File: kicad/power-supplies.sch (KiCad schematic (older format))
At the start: 16 parts, among them J2 BARREL_JACK, U3 AP3211

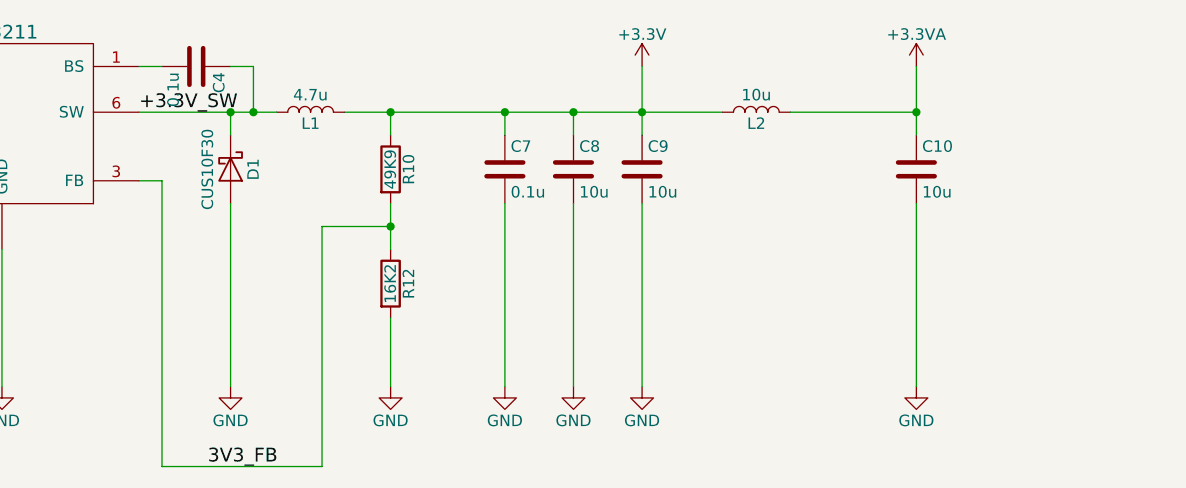
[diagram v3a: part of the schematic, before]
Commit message: Removed comp, efuse. Added zener protection. Fixed OLED footprint.
I may have destroyed a board by shorting the FB pin to ground. I left
off the zener protection on Rev A. Never again.
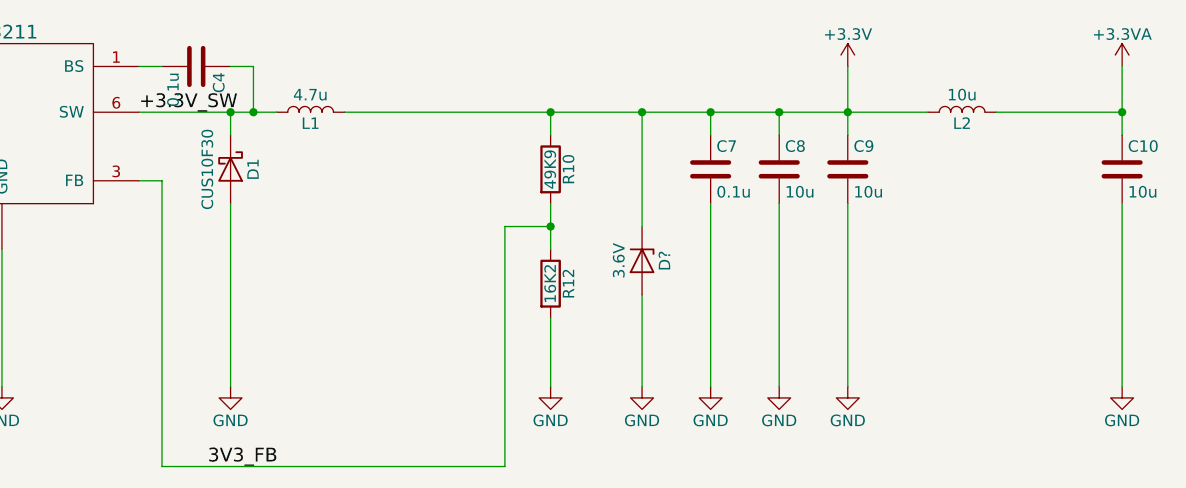
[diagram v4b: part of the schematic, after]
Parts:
- added D?: 3.6V, Diodes_SMD:D_SOD-523, symbol D_Zener
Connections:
- net +3V3: now also D?.1 (K)
- net GND: now also D?.2 (A)
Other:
- moved on the sheet: C10, C7, C8, C9, L2, R10, R12

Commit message: Added overvoltage protection circuit to +3.3V
Part selection is complete. There are things without part numbers.

It uses a TL431 as a precision comparator with integrated voltage
reference to activate a latch which both shuts down the regulator and
throws a crobar across +3.3V. There is also space for a fuse on +3.3V
(I'm thinking a PTC resettable fuse could go there, but I'm not sure
what the tradeoffs are for that).
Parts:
- added D4: NYC228STT1G, TO_SOT_Packages_SMD:SOT-223-3Lead_TabPin2, symbol Q_Thyristor_KAG
- added F1: Fuse_Small, symbol Fuse_Small
- added Q4: Q_PNP_BCE, symbol Q_PNP_BCE
- added Q5: FDG6301N_F085, TO_SOT_Packages_SMD:SOT-363_SC-70-6, symbol Q_NMOS_SGD_DUAL
- added R21, R23, R24, R25: 10K, Resistors_SMD:R_0402, symbol R
- added R22: 1K, symbol R
- added R26: 22K6, Resistors_SMD:R_0402, symbol R
- added U7: TL431, TO_SOT_Packages_SMD:SOT-323_SC-70, symbol TL431
- gave numbers to parts that had none: 1
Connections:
- net +12V: now also Q4.3 (E), R21.1
- net +3V3: now also D4.2 (A), F1.2, R24.1; no longer L1.2
- net GND: now also D4.1 (K), Q5.1 (S), Q5.4 (S), R25.2, R26.2, U7.6
- net +3.3V_EN: now reaches R11.1, R9.2, U3.4 (EN)
- net +3.3V_EN: now also Q5.6 (D)
- new net: F1.1, L1.2
- new net: Q4.2 (C), R23.1
- new net OVP_LATCH_IN: Q4.1 (B), R21.2, R22.1
- new net OVP_LATCH_OUT: D4.3 (G), Q5.2 (G), Q5.5 (G), R23.2, R25.1
- new net OVP_LATCH_REG: Q5.3 (D), R22.2, U7.1
- new net OVP_LATCH_TRIP: R24.2, R26.1, U7.3
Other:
- note added: "Alternate mosfet part: 2N7002DWCT-ND"
- note added: "Trip point 3.6V"
- note added: "Zener is optional and is a fallback if the OVP circuit does not operate\nas expected.\n\nThe OVP circuit uses a TL431 as a precision comparator with integrated\nvoltage reference to set off a latch which both disables EN and throws\nan SCR crowbar on +3.3V until 12V is removed."

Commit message: Added overtemperature latching circuit with reset
This uses a comparator to trigger the same latch type that is used on
the OVP circuit.
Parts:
- R22: footprint (none) -> Resistors_SMD:R_0402; Part No. (none) -> 311-1.0KJRCT-ND
- U7: footprint TO_SOT_Packages_SMD:SOT-323_SC-70 -> TO_SOT_Packages_SMD:SOT-363_SC-70-6
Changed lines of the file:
@@
 $EndComp
 $Comp
-L GND #PWR22
+L GND #PWR023
 U 1 1 592084EC
 P 1600 1900
-F 0 "#PWR22" H 1600 1650 50  0001 C CNN
+F 0 "#PWR023" H 1600 1650 50  0001 C CNN
 F 1 "GND" H 1600 1750 50  0000 C CNN
 F 2 "" H 1600 1900 50  0001 C CNN
@@
 $EndComp
 $Comp
-L +12V #PWR21
+L +12V #PWR024
 U 1 1 59208505
 P 1600 1200
-F 0 "#PWR21" H 1600 1050 50  0001 C CNN
+F 0 "#PWR024" H 1600 1050 50  0001 C CNN
 F 1 "+12V" H 1600 1340 50  0000 C CNN
 F 2 "" H 1600 1200 50  0001 C CNN
@@
 $EndComp
 $Comp
-L GND #PWR27
+L GND #PWR025
 U 1 1 592088C5
 P 5500 2500
-F 0 "#PWR27" H 5500 2250 50  0001 C CNN
+F 0 "#PWR025" H 5500 2250 50  0001 C CNN
 F 1 "GND" H 5500 2350 50  0000 C CNN
 F 2 "" H 5500 2500 50  0001 C CNN
@@
 $EndComp
 $Comp
-L GND #PWR26
+L GND #PWR026
 U 1 1 59208941
 P 4500 2500
-F 0 "#PWR26" H 4500 2250 50  0001 C CNN
+F 0 "#PWR026" H 4500 2250 50  0001 C CNN
 F 1 "GND" H 4500 2350 50  0000 C CNN
 F 2 "" H 4500 2500 50  0001 C CNN
@@
 $EndComp
 $Comp
-L +3.3V #PWR19
+L +3.3V #PWR027
 U 1 1 59208C89
 P 8200 1100
-F 0 "#PWR19" H 8200 950 50  0001 C CNN
+F 0 "#PWR027" H 8200 950 50  0001 C CNN
 F 1 "+3.3V" H 8200 1240 50  0000 C CNN
 F 2 "" H 8200 1100 50  0001 C CNN
@@
 $EndComp
 $Comp
-L GND #PWR32
+L GND #PWR028
 U 1 1 59208D24
 P 8200 2500
-F 0 "#PWR32" H 8200 2250 50  0001 C CNN
+F 0 "#PWR028" H 8200 2250 50  0001 C CNN
 F 1 "GND" H 8200 2350 50  0000 C CNN
 F 2 "" H 8200 2500 50  0001 C CNN
@@
 $EndComp
 $Comp
-L GND #PWR23
+L GND #PWR029
 U 1 1 59208EA1
 P 3150 2500
-F 0 "#PWR23" H 3150 2250 50  0001 C CNN
+F 0 "#PWR029" H 3150 2250 50  0001 C CNN
 F 1 "GND" H 3150 2350 50  0000 C CNN
 F 2 "" H 3150 2500 50  0001 C CNN
@@
 $EndComp
 $Comp
-L GND #PWR30
+L GND #PWR030
 U 1 1 5920907B
 P 7600 2500
-F 0 "#PWR30" H 7600 2250 50  0001 C CNN
+F 0 "#PWR030" H 7600 2250 50  0001 C CNN
 F 1 "GND" H 7600 2350 50  0000 C CNN
 F 2 "" H 7600 2500 50  0001 C CNN
@@
 $EndComp
 $Comp
-L GND #PWR24
+L GND #PWR031
 U 1 1 592091A5
 P 3400 2500
-F 0 "#PWR24" H 3400 2250 50  0001 C CNN
+F 0 "#PWR031" H 3400 2250 50  0001 C CNN
 F 1 "GND" H 3400 2350 50  0000 C CNN
 F 2 "" H 3400 2500 50  0001 C CNN
@@
 $EndComp
 $Comp
-L GND #PWR28
+L GND #PWR032
 U 1 1 592093A2
 P 6900 2500
-F 0 "#PWR28" H 6900 2250 50  0001 C CNN
+F 0 "#PWR032" H 6900 2250 50  0001 C CNN
 F 1 "GND" H 6900 2350 50  0000 C CNN
 F 2 "" H 6900 2500 50  0001 C CNN
@@
 $EndComp
 $Comp
-L GND #PWR25
+L GND #PWR033
 U 1 1 59209C78
 P 3700 2500
-F 0 "#PWR25" H 3700 2250 50  0001 C CNN
+F 0 "#PWR033" H 3700 2250 50  0001 C CNN
 F 1 "GND" H 3700 2350 50  0000 C CNN
 F 2 "" H 3700 2500 50  0001 C CNN
@@
 $EndComp
 $Comp
-L GND #PWR31
+L GND #PWR034
 U 1 1 5920A4A0
 P 7900 2500
-F 0 "#PWR31" H 7900 2250 50  0001 C CNN
+F 0 "#PWR034" H 7900 2250 50  0001 C CNN
 F 1 "GND" H 7900 2350 50  0000 C CNN
 F 2 "" H 7900 2500 50  0001 C CNN
@@
 $EndComp
 $Comp
-L GND #PWR33
+L GND #PWR035
 U 1 1 592C8FE8
 P 9400 2500
-F 0 "#PWR33" H 9400 2250 50  0001 C CNN
+F 0 "#PWR035" H 9400 2250 50  0001 C CNN
 F 1 "GND" H 9400 2350 50  0000 C CNN
 F 2 "" H 9400 2500 50  0001 C CNN
@@
 $EndComp
 $Comp
-L +3.3VA #PWR20
+L +3.3VA #PWR036
 U 1 1 592C9106
 P 9400 1100
-F 0 "#PWR20" H 9400 950 50  0001 C CNN
+F 0 "#PWR036" H 9400 950 50  0001 C CNN
 F 1 "+3.3VA" H 9400 1240 50  0000 C CNN
 F 2 "" H 9400 1100 50  0001 C CNN
@@
 $EndComp
 $Comp
-L GND #PWR29
+L GND #PWR037
 U 1 1 5987D189
 P 7300 2500
-F 0 "#PWR29" H 7300 2250 50  0001 C CNN
+F 0 "#PWR037" H 7300 2250 50  0001 C CNN
 F 1 "GND" H 7300 2350 50  0000 C CNN
 F 2 "" H 7300 2500 50  0001 C CNN
@@
 F 0 "U7" H 2300 4950 60  0000 C CNN
 F 1 "TL431" H 2400 5300 60  0000 C CNN
-F 2 "TO_SOT_Packages_SMD:SOT-323_SC-70" H 2200 5150 60  0001 C CNN
+F 2 "TO_SOT_Packages_SMD:SOT-363_SC-70-6" H 2200 5150 60  0001 C CNN
 F 3 "" H 2200 5150 60  0001 C CNN
 F 4 "296-17863-1-ND" H 2200 5150 60  0001 C CNN "Part No."
@@
 F 0 "R22" V 2280 4550 50  0000 C CNN
 F 1 "1K" V 2200 4550 50  0000 C CNN
-F 2 "" V 2130 4550 50  0001 C CNN
+F 2 "Resistors_SMD:R_0402" V 2130 4550 50  0001 C CNN
 F 3 "" H 2200 4550 50  0001 C CNN
+F 4 "311-1.0KJRCT-ND" H 2200 4550 60  0001 C CNN "Part No."
 	1    2200 4550
 	-1   0    0    -1
 $EndComp
 $Comp
-L GND #PWR37
+L GND #PWR038
 U 1 1 5998FEAD
 P 2200 5800
-F 0 "#PWR37" H 2200 5550 50  0001 C CNN
+F 0 "#PWR038" H 2200 5550 50  0001 C CNN
 F 1 "GND" H 2200 5650 50  0000 C CNN
 F 2 "" H 2200 5800 50  0001 C CNN
@@
 Trip point 3.6V
 $Comp
-L +12V #PWR34
+L +12V #PWR039
 U 1 1 599906B9
 P 3600 3700
-F 0 "#PWR34" H 3600 3550 50  0001 C CNN
+F 0 "#PWR039" H 3600 3550 50  0001 C CNN
 F 1 "+12V" H 3600 3840 50  0000 C CNN
 F 2 "" H 3600 3700 50  0001 C CNN
@@
 $EndComp
 $Comp
-L +3.3V #PWR36
+L +3.3V #PWR040
 U 1 1 59991F79
 P 1700 4600
-F 0 "#PWR36" H 1700 4450 50  0001 C CNN
+F 0 "#PWR040" H 1700 4450 50  0001 C CNN
 F 1 "+3.3V" H 1700 4740 50  0000 C CNN
 F 2 "" H 1700 4600 50  0001 C CNN
@@
 	1600 1200 1600 1300
 Wire Wire Line
-	5100 1300 5500 1300
-Wire Wire Line
-	5500 1300 5600 1300
-Wire Wire Line
-	5600 1300 5700 1300
+	5100 1300 5700 1300
 Wire Wire Line
 	5200 1100 5100 1100
@@
 	1500 1500 1600 1500
 Wire Wire Line
-	1500 1300 1600 1300
-Wire Wire Line
-	1600 1300 3150 1300
-Wire Wire Line
-	3150 1300 3400 1300
-Wire Wire Line
-	3400 1300 3700 1300
-Wire Wire Line
-	3700 1300 3900 1300
+	1500 1300 3900 1300
 Wire Wire Line
 	4500 2500 4500 1900
 Connection ~ 1600 1300
 Wire Wire Line
-	8200 1100 8200 1300
-Wire Wire Line
-	8200 1300 8200 1400
+	8200 1100 8200 1400
 Connection ~ 7900 1300
 Wire Wire Line
@@
 Connection ~ 3150 1300
 Wire Wire Line
-	7600 1400 7600 1300
+	7600 1300 7600 1400
 Connection ~ 7600 1300
 Wire Wire Line
@@
 	6900 2500 6900 2200
 Wire Wire Line
-	6900 1700 6900 1800
-Wire Wire Line
-	6900 1800 6900 1900
+	6900 1700 6900 1900
 Wire Wire Line
 	6900 1400 6900 1300
@@
 	3700 1300 3700 1400
 Wire Wire Line
-	3700 1700 3700 1800
-Wire Wire Line
-	3700 1800 3700 1900
+	3700 1700 3700 1900
 Wire Wire Line
 	3700 2500 3700 2200
@@
 Connection ~ 8200 1300
 Wire Wire Line
-	7900 1400 7900 1300
+	7900 1300 7900 1400
 Wire Wire Line
 	7900 2500 7900 1700
 Wire Wire Line
-	9400 1100 9400 1300
-Wire Wire Line
-	9400 1300 9400 1400
+	9400 1100 9400 1400
 Wire Wire Line
 	9400 1700 9400 2500
@@
 Connection ~ 9400 1300
 Wire Wire Line
-	7300 1800 7300 1300
+	7300 1300 7300 1800
 Connection ~ 7300 1300
 Wire Wire Line
@@
 	3300 4300 2200 4300
 Wire Wire Line
-	2200 4200 2200 4300
-Wire Wire Line
-	2200 4300 2200 4400
-Wire Wire Line
-	2200 4700 2200 4800
-Wire Wire Line
-	2200 4800 2200 4850
-Wire Wire Line
-	2200 5500 2200 5600
-Wire Wire Line
-	2200 5600 2200 5700
-Wire Wire Line
-	2200 5700 2200 5800
+	2200 4200 2200 4400
+Wire Wire Line
+	2200 4700 2200 4850
+Wire Wire Line
+	2200 5500 2200 5800
 Wire Wire Line
 	2200 5700 1700 5700
@@
 	1900 5200 1700 5200
 Wire Wire Line
-	1700 5100 1700 5200
-Wire Wire Line
-	1700 5200 1700 5300
+	1700 5100 1700 5300
 Connection ~ 1700 5200
 Wire Wire Line
-	3600 3700 3600 3800
-Wire Wire Line
-	3600 3800 3600 4100
+	3600 3700 3600 4100
 Wire Wire Line
 	3600 3800 2200 3800
@@
 Connection ~ 2200 4300
 Wire Wire Line
-	2200 5600 3000 5600
-Wire Wire Line
-	3000 5600 3600 5600
-Wire Wire Line
-	3600 5600 4900 5600
-Wire Wire Line
-	4900 5600 5750 5600
+	2200 5600 5750 5600
 Wire Wire Line
 	3600 5600 3600 5500
@@
 Connection ~ 3000 5600
 Wire Wire Line
-	3600 4900 3600 5000
-Wire Wire Line
-	3600 5000 3600 5100
-Wire Wire Line
-	3600 5100 3600 5200
+	3600 4900 3600 5200
 Wire Wire Line
 	3600 5100 3300 5100
@@
 Connection ~ 3600 5600
 Wire Wire Line
-	3600 5000 4600 5000
-Wire Wire Line
-	4600 5000 5600 5000
+	3600 5000 5600 5000
 Connection ~ 3600 5000
 Wire Wire Line
@@
 $EndComp
 $Comp
-L +3.3V #PWR35
+L +3.3V #PWR041
 U 1 1 599981D4
 P 5750 4400
-F 0 "#PWR35" H 5750 4250 50  0001 C CNN
+F 0 "#PWR041" H 5750 4250 50  0001 C CNN
 F 1 "+3.3V" H 5750 4540 50  0000 C CNN
 F 2 "" H 5750 4400 50  0001 C CNN
@@
 	5750 4400 5750 4750
 Wire Wire Line
-	3850 1600 3850 1800
-Wire Wire Line
-	3850 1800 3850 2900
+	3850 1600 3850 2900
 Wire Wire Line
 	4900 4800 4900 2900
@@
 	6000 1300 6200 1300
 Wire Wire Line
-	6400 1300 6900 1300
-Wire Wire Line
-	6900 1300 7300 1300
-Wire Wire Line
-	7300 1300 7600 1300
-Wire Wire Line
-	7600 1300 7900 1300
-Wire Wire Line
-	7900 1300 8200 1300
-Wire Wire Line
-	8200 1300 8550 1300
+	6400 1300 8550 1300
 Text Notes 6300 4200 0    60   ~ 0
 Zener is optional and is a fallback if the OVP circuit does not operate\nas expected.\n\nThe OVP circuit uses a TL431 as a precision comparator with integrated\nvoltage reference to set off a latch which both disables EN and throws\nan SCR crowbar on +3.3V until 12V is removed.

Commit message: Fixed thermal cutoff circuit and finished footprint selection
The main issue with the thermal cutoff was the open-collector maximum
voltage. I had to find a (slightly more expensive) comparator with an
output that was tolerant. Other comparators that would be instead
tolerant of being run off 12V were about the same price.

The fuse I'm not sure about. I'm just going to short it out. The
regulator can handle a short circuit and so can the crowbar. I also
couldn't decide where to put the feedback network. If I put it after the
fuse it would compensate for any voltage drop across it. However, it
would also cause the regulator to try to boost the voltage insanely high
during a short circuit across the fuse and maybe cause it to pop (I
could really only find ones rated to 6V). I instead placed it before the
fuse. I'm still not sure.
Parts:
- removed Q4: Q_PNP_BCE, symbol Q_PNP_BCE
- added Q4: MMBT3906WT1G, TO_SOT_Packages_SMD:SOT-323_SC-70, symbol Q_PNP_BEC
- F1: footprint (none) -> Resistors_SMD:R_0603
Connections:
- net +12V: now also Q4.2 (E)
- net +3V3: no longer R10.1
- net OVP_LATCH_IN: now also Q4.1 (B)
- net at F1.1, L1.2: now also R10.1
- net at R23.1: now also Q4.3 (C)
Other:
- note added: "The fuse here is probably optional. I will replace it with\na short, but the 0603 footprint should allow a standard\nSMD fuse or PTC thermistor in its place.\n\nThe AP3211 should handle a short circuit condition and\nshut down. The crowbar can sustain the 1.5A maximum\ncurrent."
- moved on the sheet: C10, C4, C5, C6, C7, C8, C9, D1, D3, F1, J2, L1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

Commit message: Changed out switch for two small side clicker ones
Should make things a little easier to lay out and easier to modify
later.
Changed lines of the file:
@@
 $EndComp
 $Comp
-L GND #PWR023
+L GND #PWR26
 U 1 1 592084EC
 P 1600 2100
-F 0 "#PWR023" H 1600 1850 50  0001 C CNN
+F 0 "#PWR26" H 1600 1850 50  0001 C CNN
 F 1 "GND" H 1600 1950 50  0000 C CNN
 F 2 "" H 1600 2100 50  0001 C CNN
@@
 $EndComp
 $Comp
-L +12V #PWR024
+L +12V #PWR25
 U 1 1 59208505
 P 1600 1400
-F 0 "#PWR024" H 1600 1250 50  0001 C CNN
+F 0 "#PWR25" H 1600 1250 50  0001 C CNN
 F 1 "+12V" H 1600 1540 50  0000 C CNN
 F 2 "" H 1600 1400 50  0001 C CNN
@@
 $EndComp
 $Comp
-L GND #PWR025
+L GND #PWR31
 U 1 1 592088C5
 P 5500 2700
-F 0 "#PWR025" H 5500 2450 50  0001 C CNN
+F 0 "#PWR31" H 5500 2450 50  0001 C CNN
 F 1 "GND" H 5500 2550 50  0000 C CNN
 F 2 "" H 5500 2700 50  0001 C CNN
@@
 $EndComp
 $Comp
-L GND #PWR026
+L GND #PWR30
 U 1 1 59208941
 P 4500 2700
-F 0 "#PWR026" H 4500 2450 50  0001 C CNN
+F 0 "#PWR30" H 4500 2450 50  0001 C CNN
 F 1 "GND" H 4500 2550 50  0000 C CNN
 F 2 "" H 4500 2700 50  0001 C CNN
@@
 $EndComp
 $Comp
-L +3.3V #PWR027
+L +3.3V #PWR23
 U 1 1 59208C89
 P 8200 1300
-F 0 "#PWR027" H 8200 1150 50  0001 C CNN
+F 0 "#PWR23" H 8200 1150 50  0001 C CNN
 F 1 "+3.3V" H 8200 1440 50  0000 C CNN
 F 2 "" H 8200 1300 50  0001 C CNN
@@
 $EndComp
 $Comp
-L GND #PWR028
+L GND #PWR36
 U 1 1 59208D24
 P 8200 2700
-F 0 "#PWR028" H 8200 2450 50  0001 C CNN
+F 0 "#PWR36" H 8200 2450 50  0001 C CNN
 F 1 "GND" H 8200 2550 50  0000 C CNN
 F 2 "" H 8200 2700 50  0001 C CNN
@@
 $EndComp
 $Comp
-L GND #PWR029
+L GND #PWR27
 U 1 1 59208EA1
 P 3150 2700
-F 0 "#PWR029" H 3150 2450 50  0001 C CNN
+F 0 "#PWR27" H 3150 2450 50  0001 C CNN
 F 1 "GND" H 3150 2550 50  0000 C CNN
 F 2 "" H 3150 2700 50  0001 C CNN
@@
 $EndComp
 $Comp
-L GND #PWR030
+L GND #PWR34
 U 1 1 5920907B
 P 7600 2700
-F 0 "#PWR030" H 7600 2450 50  0001 C CNN
+F 0 "#PWR34" H 7600 2450 50  0001 C CNN
 F 1 "GND" H 7600 2550 50  0000 C CNN
 F 2 "" H 7600 2700 50  0001 C CNN
@@
 $EndComp
 $Comp
-L GND #PWR031
+L GND #PWR28
 U 1 1 592091A5
 P 3400 2700
-F 0 "#PWR031" H 3400 2450 50  0001 C CNN
+F 0 "#PWR28" H 3400 2450 50  0001 C CNN
 F 1 "GND" H 3400 2550 50  0000 C CNN
 F 2 "" H 3400 2700 50  0001 C CNN
@@
 $EndComp
 $Comp
-L GND #PWR032
+L GND #PWR32
 U 1 1 592093A2
 P 6100 2700
-F 0 "#PWR032" H 6100 2450 50  0001 C CNN
+F 0 "#PWR32" H 6100 2450 50  0001 C CNN
 F 1 "GND" H 6100 2550 50  0000 C CNN
 F 2 "" H 6100 2700 50  0001 C CNN
@@
 $EndComp
 $Comp
-L GND #PWR033
+L GND #PWR29
 U 1 1 59209C78
 P 3700 2700
-F 0 "#PWR033" H 3700 2450 50  0001 C CNN
+F 0 "#PWR29" H 3700 2450 50  0001 C CNN
 F 1 "GND" H 3700 2550 50  0000 C CNN
 F 2 "" H 3700 2700 50  0001 C CNN
@@
 $EndComp
 $Comp
-L GND #PWR034
+L GND #PWR35
 U 1 1 5920A4A0
 P 7900 2700
-F 0 "#PWR034" H 7900 2450 50  0001 C CNN
+F 0 "#PWR35" H 7900 2450 50  0001 C CNN
 F 1 "GND" H 7900 2550 50  0000 C CNN
 F 2 "" H 7900 2700 50  0001 C CNN
@@
 $EndComp
 $Comp
-L GND #PWR035
+L GND #PWR37
 U 1 1 592C8FE8
 P 9400 2700
-F 0 "#PWR035" H 9400 2450 50  0001 C CNN
+F 0 "#PWR37" H 9400 2450 50  0001 C CNN
 F 1 "GND" H 9400 2550 50  0000 C CNN
 F 2 "" H 9400 2700 50  0001 C CNN
@@
 $EndComp
 $Comp
-L +3.3VA #PWR036
+L +3.3VA #PWR24
 U 1 1 592C9106
 P 9400 1300
-F 0 "#PWR036" H 9400 1150 50  0001 C CNN
+F 0 "#PWR24" H 9400 1150 50  0001 C CNN
 F 1 "+3.3VA" H 9400 1440 50  0000 C CNN
 F 2 "" H 9400 1300 50  0001 C CNN
@@
 $EndComp
 $Comp
-L GND #PWR037
+L GND #PWR33
 U 1 1 5987D189
 P 7300 2700
-F 0 "#PWR037" H 7300 2450 50  0001 C CNN
+F 0 "#PWR33" H 7300 2450 50  0001 C CNN
 F 1 "GND" H 7300 2550 50  0000 C CNN
 F 2 "" H 7300 2700 50  0001 C CNN
@@
 $EndComp
 $Comp
-L GND #PWR038
+L GND #PWR41
 U 1 1 5998FEAD
 P 2200 5800
-F 0 "#PWR038" H 2200 5550 50  0001 C CNN
+F 0 "#PWR41" H 2200 5550 50  0001 C CNN
 F 1 "GND" H 2200 5650 50  0000 C CNN
 F 2 "" H 2200 5800 50  0001 C CNN
@@
 Trip point 3.6V
 $Comp
-L +12V #PWR039
+L +12V #PWR38
 U 1 1 599906B9
 P 3600 3700
-F 0 "#PWR039" H 3600 3550 50  0001 C CNN
+F 0 "#PWR38" H 3600 3550 50  0001 C CNN
 F 1 "+12V" H 3600 3840 50  0000 C CNN
 F 2 "" H 3600 3700 50  0001 C CNN
@@
 $EndComp
 $Comp
-L +3.3V #PWR040
+L +3.3V #PWR40
 U 1 1 59991F79
 P 1700 4600
-F 0 "#PWR040" H 1700 4450 50  0001 C CNN
+F 0 "#PWR40" H 1700 4450 50  0001 C CNN
 F 1 "+3.3V" H 1700 4740 50  0000 C CNN
 F 2 "" H 1700 4600 50  0001 C CNN
@@
 	1600 1400 1600 1500
 Wire Wire Line
-	5100 1500 5500 1500
-Wire Wire Line
-	5500 1500 5600 1500
-Wire Wire Line
-	5600 1500 5700 1500
+	5100 1500 5700 1500
 Wire Wire Line
 	5200 1300 5100 1300
@@
 	1500 1700 1600 1700
 Wire Wire Line
-	1500 1500 1600 1500
-Wire Wire Line
-	1600 1500 3150 1500
-Wire Wire Line
-	3150 1500 3400 1500
-Wire Wire Line
-	3400 1500 3700 1500
-Wire Wire Line
-	3700 1500 3900 1500
+	1500 1500 3900 1500
 Wire Wire Line
 	4500 2700 4500 2100
 Connection ~ 1600 1500
 Wire Wire Line
-	8200 1300 8200 1500
-Wire Wire Line
-	8200 1500 8200 1600
+	8200 1300 8200 1600
 Connection ~ 7900 1500
 Wire Wire Line
@@
 	6100 2700 6100 2400
 Wire Wire Line
-	6100 1900 6100 2000
-Wire Wire Line
-	6100 2000 6100 2100
+	6100 1900 6100 2100
 Wire Wire Line
 	6100 1600 6100 1500
@@
 	3700 1500 3700 1600
 Wire Wire Line
-	3700 1900 3700 2000
-Wire Wire Line
-	3700 2000 3700 2100
+	3700 1900 3700 2100
 Wire Wire Line
 	3700 2700 3700 2400
@@
 	7900 2700 7900 1900
 Wire Wire Line
-	9400 1300 9400 1500
-Wire Wire Line
-	9400 1500 9400 1600
+	9400 1300 9400 1600
 Wire Wire Line
 	9400 1900 9400 2700
@@
 	3300 4300 2200 4300
 Wire Wire Line
-	2200 4200 2200 4300
-Wire Wire Line
-	2200 4300 2200 4400
-Wire Wire Line
-	2200 4700 2200 4800
-Wire Wire Line
-	2200 4800 2200 4850
-Wire Wire Line
-	2200 5500 2200 5600
-Wire Wire Line
-	2200 5600 2200 5700
-Wire Wire Line
-	2200 5700 2200 5800
+	2200 4200 2200 4400
+Wire Wire Line
+	2200 4700 2200 4850
+Wire Wire Line
+	2200 5500 2200 5800
 Wire Wire Line
 	2200 5700 1700 5700
@@
 	1900 5200 1700 5200
 Wire Wire Line
-	1700 5100 1700 5200
-Wire Wire Line
-	1700 5200 1700 5300
+	1700 5100 1700 5300
 Connection ~ 1700 5200
 Wire Wire Line
-	3600 3700 3600 3800
-Wire Wire Line
-	3600 3800 3600 4100
+	3600 3700 3600 4100
 Wire Wire Line
 	3600 3800 2200 3800
@@
 Connection ~ 2200 4300
 Wire Wire Line
-	2200 5600 3000 5600
-Wire Wire Line
-	3000 5600 3600 5600
-Wire Wire Line
-	3600 5600 4900 5600
-Wire Wire Line
-	4900 5600 5750 5600
+	2200 5600 5750 5600
 Wire Wire Line
 	3600 5600 3600 5500
@@
 Connection ~ 3000 5600
 Wire Wire Line
-	3600 4900 3600 5000
-Wire Wire Line
-	3600 5000 3600 5100
-Wire Wire Line
-	3600 5100 3600 5200
+	3600 4900 3600 5200
 Wire Wire Line
 	3600 5100 3300 5100
@@
 Connection ~ 3600 5600
 Wire Wire Line
-	3600 5000 4600 5000
-Wire Wire Line
-	4600 5000 5600 5000
+	3600 5000 5600 5000
 Connection ~ 3600 5000
 Wire Wire Line
@@
 $EndComp
 $Comp
-L +3.3V #PWR041
+L +3.3V #PWR39
 U 1 1 599981D4
 P 5750 4400
-F 0 "#PWR041" H 5750 4250 50  0001 C CNN
+F 0 "#PWR39" H 5750 4250 50  0001 C CNN
 F 1 "+3.3V" H 5750 4540 50  0000 C CNN
 F 2 "" H 5750 4400 50  0001 C CNN
@@
 	5750 4400 5750 4750
 Wire Wire Line
-	3850 1800 3850 2000
-Wire Wire Line
-	3850 2000 3850 3100
+	3850 1800 3850 3100
 Wire Wire Line
 	4900 4800 4900 3100
@@
 $EndComp
 Wire Wire Line
-	6000 1500 6100 1500
-Wire Wire Line
-	6100 1500 6300 1500
-Wire Wire Line
-	6500 1500 7300 1500
-Wire Wire Line
-	7300 1500 7600 1500
-Wire Wire Line
-	7600 1500 7900 1500
-Wire Wire Line
-	7900 1500 8200 1500
-Wire Wire Line
-	8200 1500 8550 1500
+	6000 1500 6300 1500
+Wire Wire Line
+	6500 1500 8550 1500
 Text Notes 5500 1200 0    60   ~ 0
 The fuse here is probably optional. I will replace it with\na short, but the 0603 footprint should allow a standard\nSMD fuse or PTC thermistor in its place.\n\nThe AP3211 should handle a short circuit condition and\nshut down. The crowbar can sustain the 1.5A maximum\ncurrent.
